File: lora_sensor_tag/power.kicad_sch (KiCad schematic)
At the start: 27 parts, among them J1 Li-ion_bat_conn, U1 MCP73871-2CAI_ML, U2 TPS63070RNMR, U3 AMS1117-3.3, U4 MAX17048G_T10

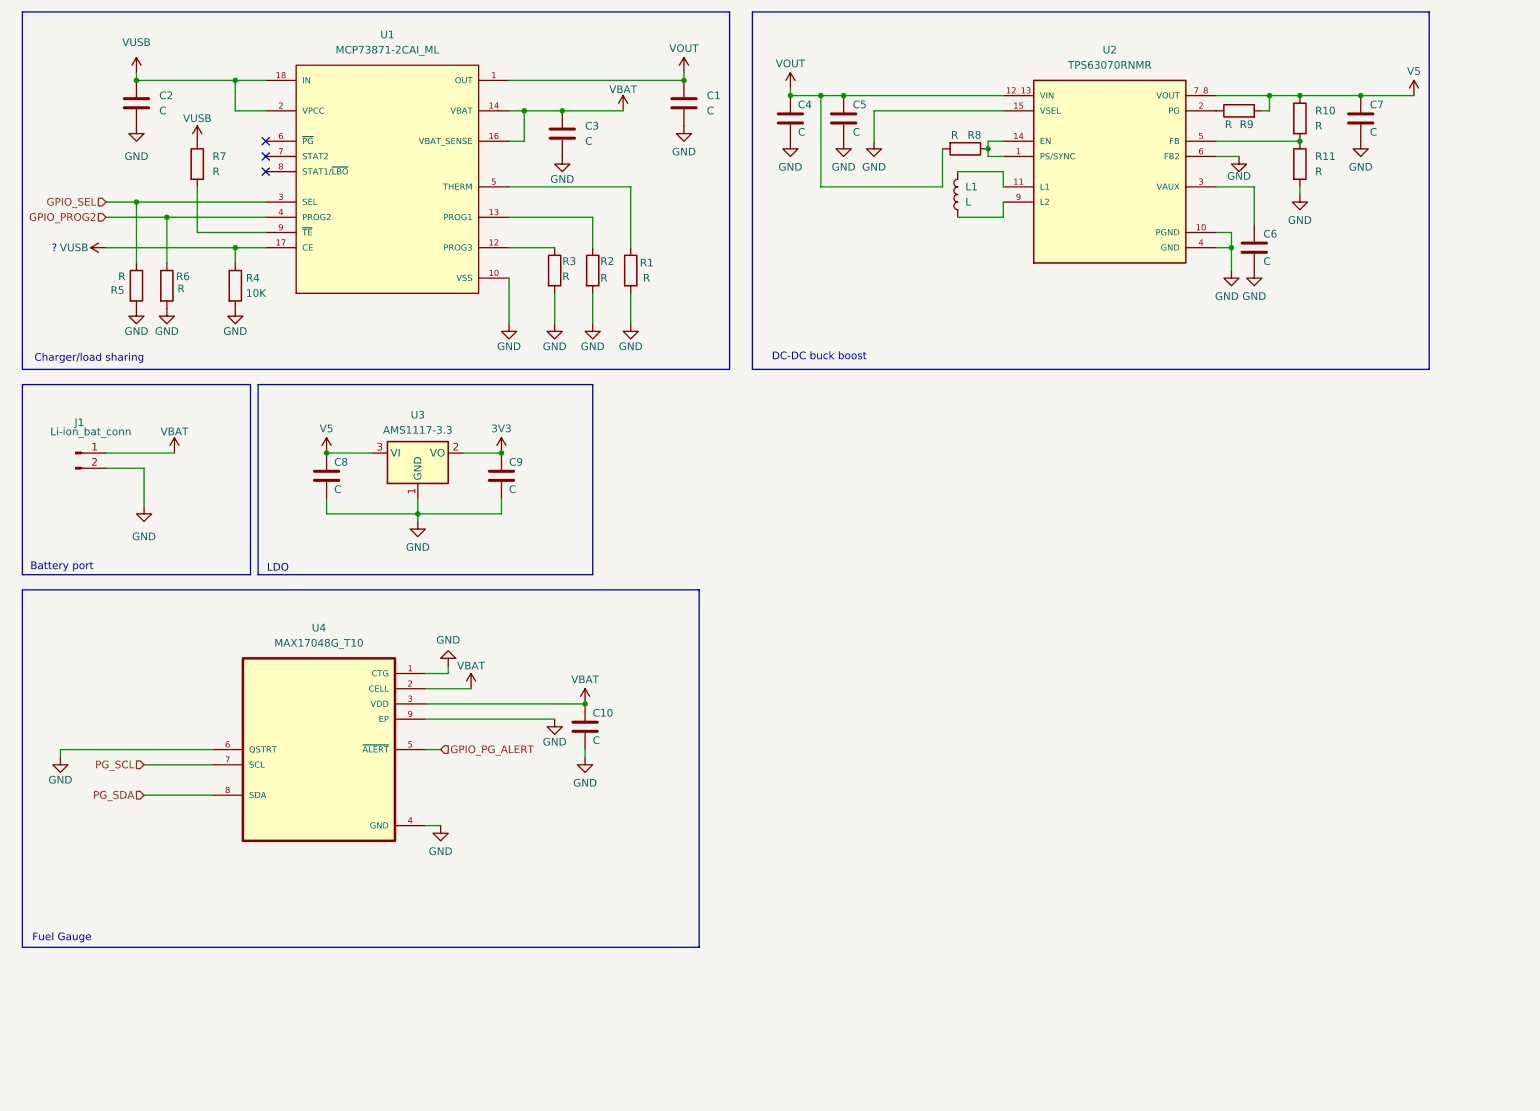
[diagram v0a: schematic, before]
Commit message: lora_sensor_tag: Update shematic
Update schematic with the following changes:
 - Add SX1276 LoRa modem schematic;
 - Add antenna matching network for SX1276 LoRa modem;
 - Add PE4259 RF switch for SX1276 LoRa modem;
 - Add USB-C connector;
 - Add CP2102 USB-to-UART bridge and programming interface;

Signed-off-by: Volodymyr <volodymyrnoha99@gmail.com>
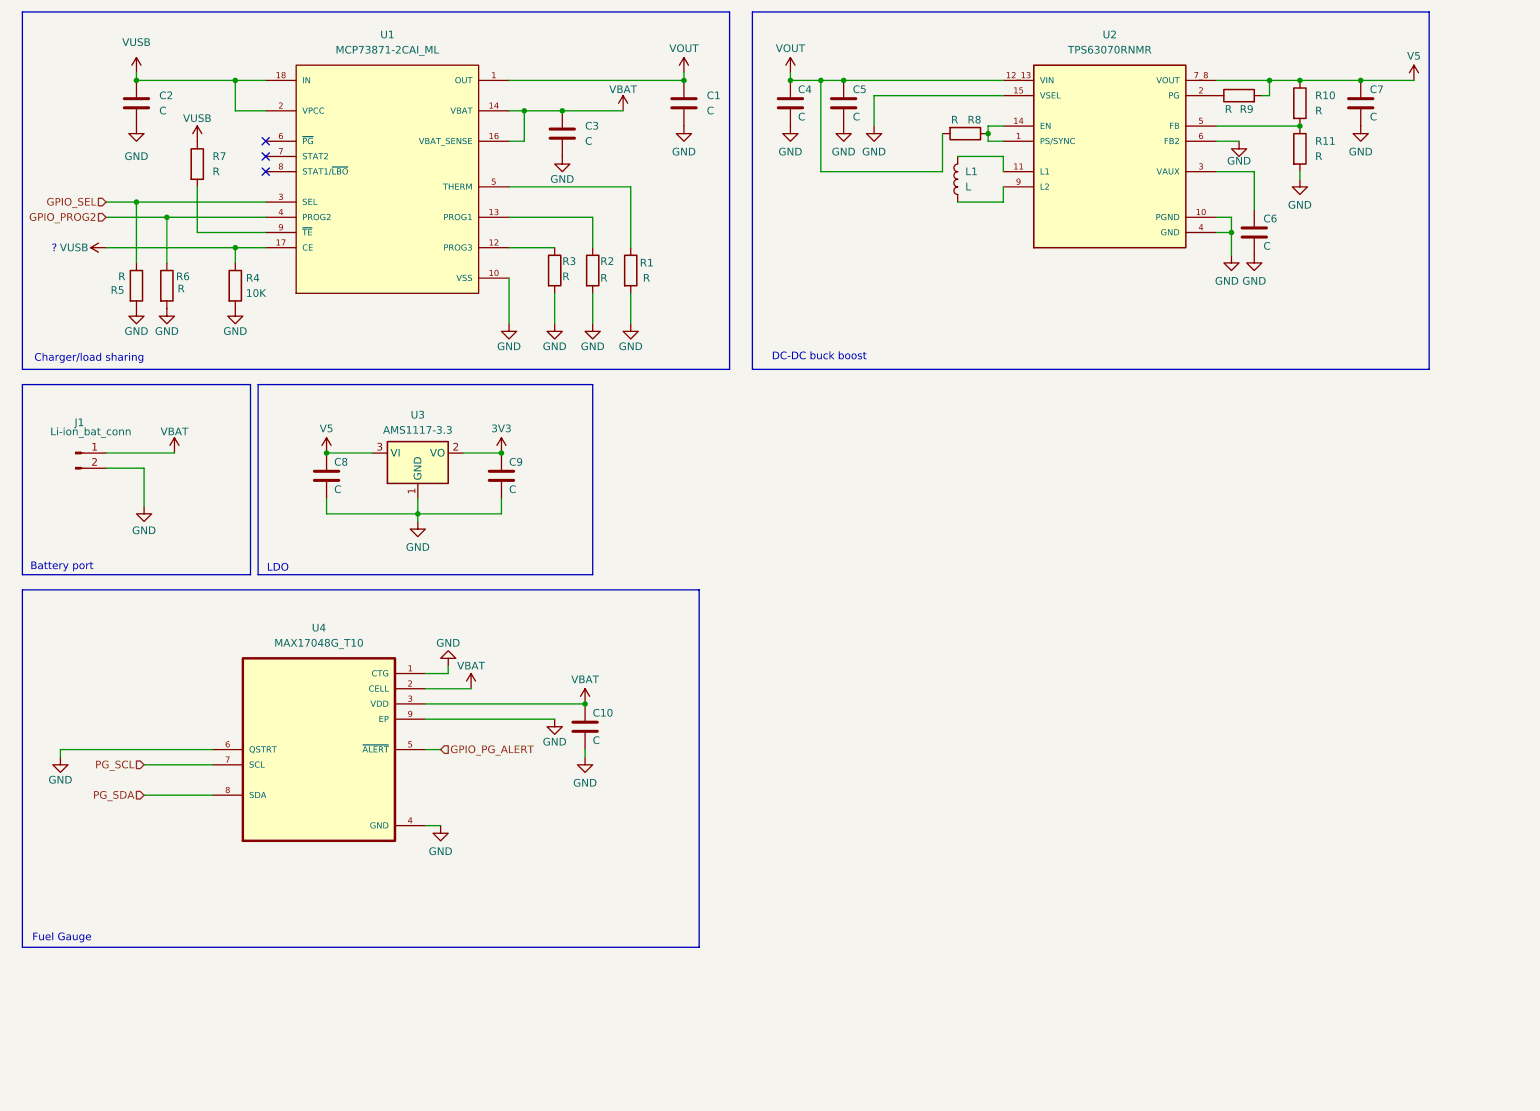
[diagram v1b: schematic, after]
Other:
- moved on the sheet: C4, C5, C6, C7, L1, R10, R11, R8, R9, U2

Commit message: Update schematic notation and fix bugs
Global labels notation updated;
Swapped line order in schematic fixed;
Added pull-up resistor to PG-ALERT pin (fuel gauge)

Signed-off-by: Volodymyr <volodymyrnoha99@gmail.com>
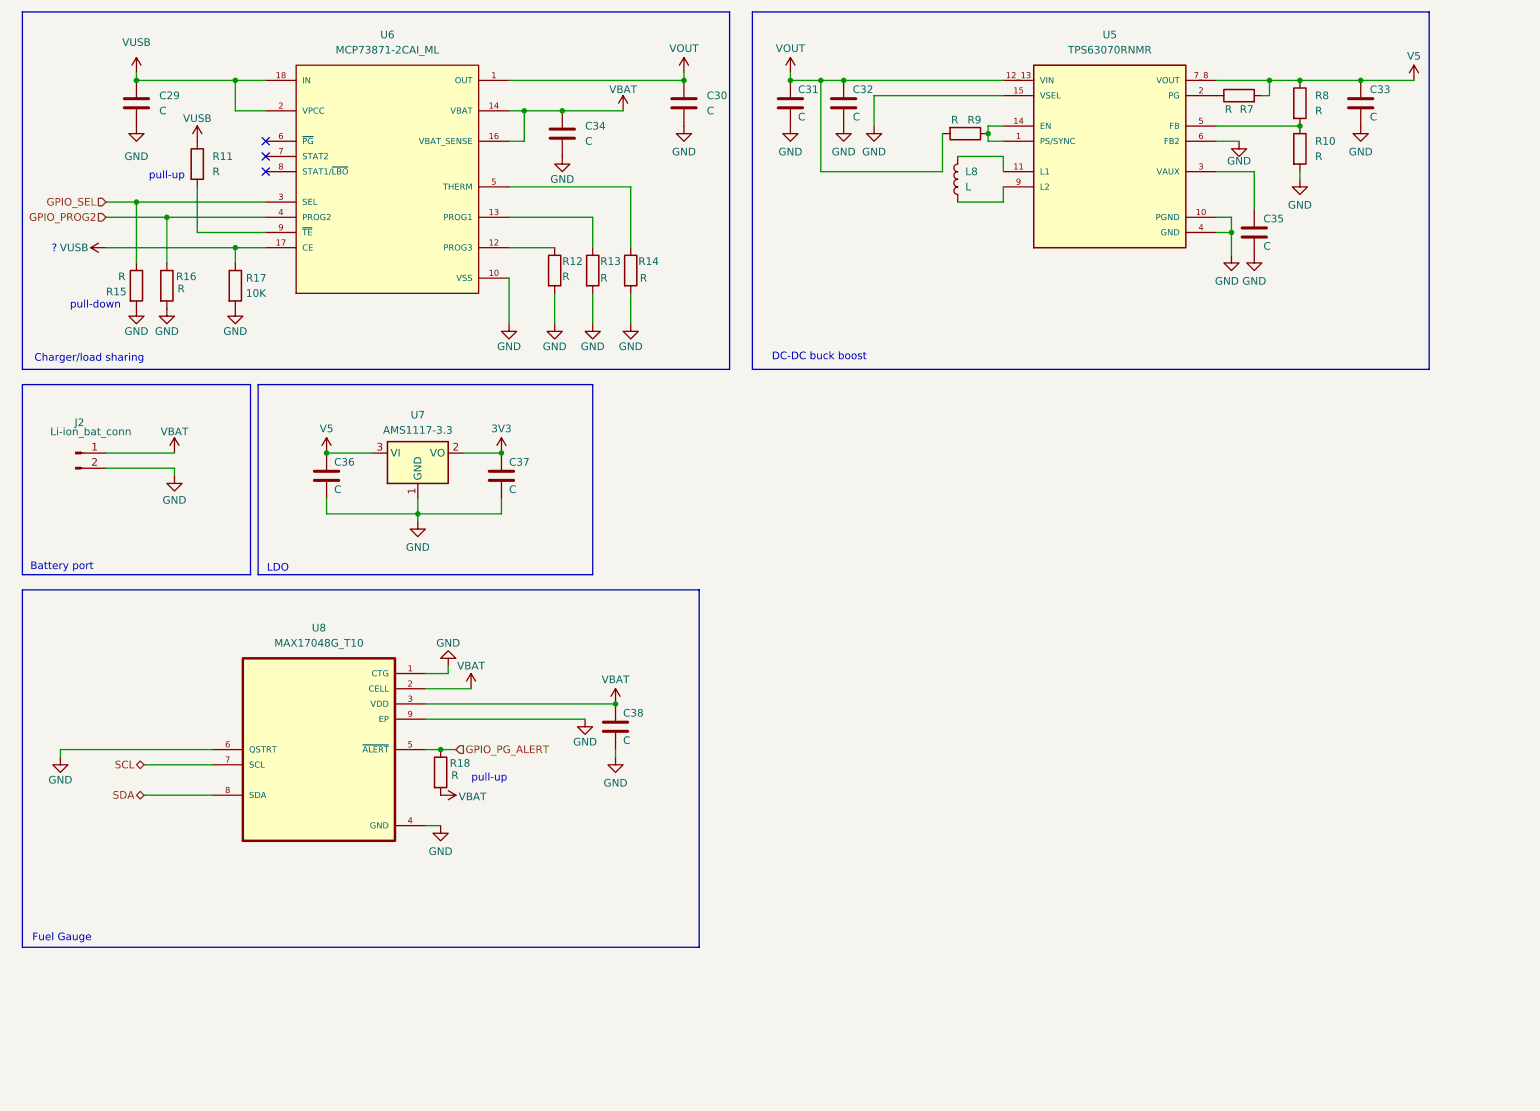
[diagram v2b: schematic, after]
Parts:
- added R18: R, TPS63070RNMR:VREG_TPS63070RNMR, symbol Device:R
- renumbered C2 to C29, C1 to C30, C4 to C31, C5 to C32, C7 to C33, C3 to C34, C6 to C35, C8 to C36, C9 to C37, C10 to C38, J1 to J2, L1 to L8, R11 to R10, R7 to R11, R3 to R12, R2 to R13, R1 to R14, R5 to R15, R6 to R16, R4 to R17, R9 to R7, R10 to R8, R8 to R9, U2 to U5, U1 to U6, U3 to U7, U4 to U8
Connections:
- net GPIO_PG_ALERT: now also R18.1
- net VBAT: now also R18.2
- net PG_SCL renamed SCL
- net PG_SDA renamed SDA
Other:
- note added: "pull-down"
- note added: "pull-up"
- title: (none) -> Power System
- moved on the sheet: C38

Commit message: Bug fixing
The following bugs and issues have been fixed:
- Fixed LoRa Rx\Tx line polarity;
- Removed unnneccessary pull-up\pull-down resistors;
- Added pull-up resistor to IO0;
- Added resistive divider for MCP7387 VPCC pin;
- GPIO_SEL moved from IO4 to IO26 (IO4 used for flash init and can cause unexpected behavior);
- CC1 and CC2 of USB-C port connected to GND via pull-down resistors;

Signed-off-by: Volodymyr <volodymyrnoha99@gmail.com>
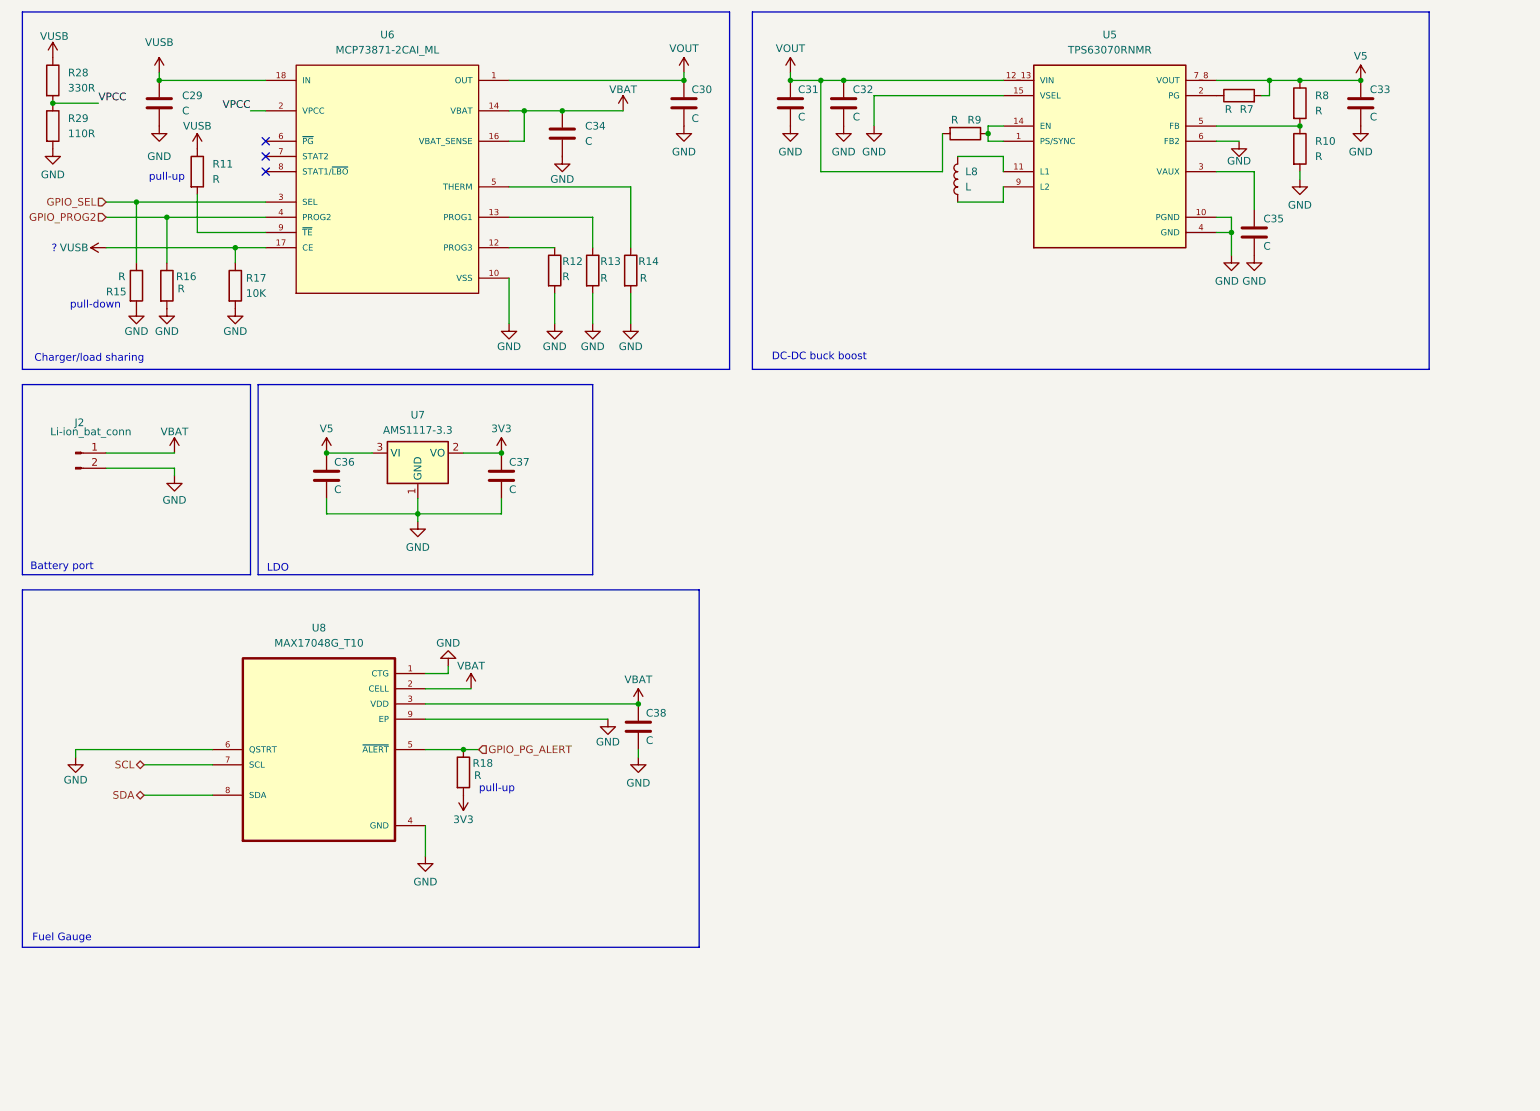
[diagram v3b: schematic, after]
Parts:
- added R28: 330R, TPS63070RNMR:VREG_TPS63070RNMR, symbol Device:R
- added R29: 110R, TPS63070RNMR:VREG_TPS63070RNMR, symbol Device:R
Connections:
- net 3V3: now also R18.2
- net GND: now also R29.2
- net VBAT: no longer R18.2
- net VUSB: now also R28.1; no longer U6.2 (VPCC)
- new net VPCC: R28.2, R29.1, U6.2 (VPCC)
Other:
- moved on the sheet: C29, C38, R11, R18

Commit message: Update Charge Enable mechanism on MCP73871
Adds the following charge enable control mechanism
on MCP73871:

VUSB ──|>|──┐
     D_CE1  │
            ├── V_CE_SRC ── R17 ──┬──── CE, U6.17
VBAT ──|>|──┘             47 кОм  │   |
     D_CE2                        C  R34
                                 │    |
GPIO26 ── R_B ──┬────────────── B Q3 GND
         47 кОм │                │
               R_BE              E   NPN
              100 кОм            │
                │               GND
               GND

This solution allows for controlled enabling of
the charge function  on the MCP73871, ensuring
that the charge enable pin is properly managed
through the diodes and transistor network.The
circuit allows control of the CE pin via the
GPIO26 pin and helps to keep CE in a proper state.

Signed-off-by: Volodymyr <volodymyrnoha99@gmail.com>
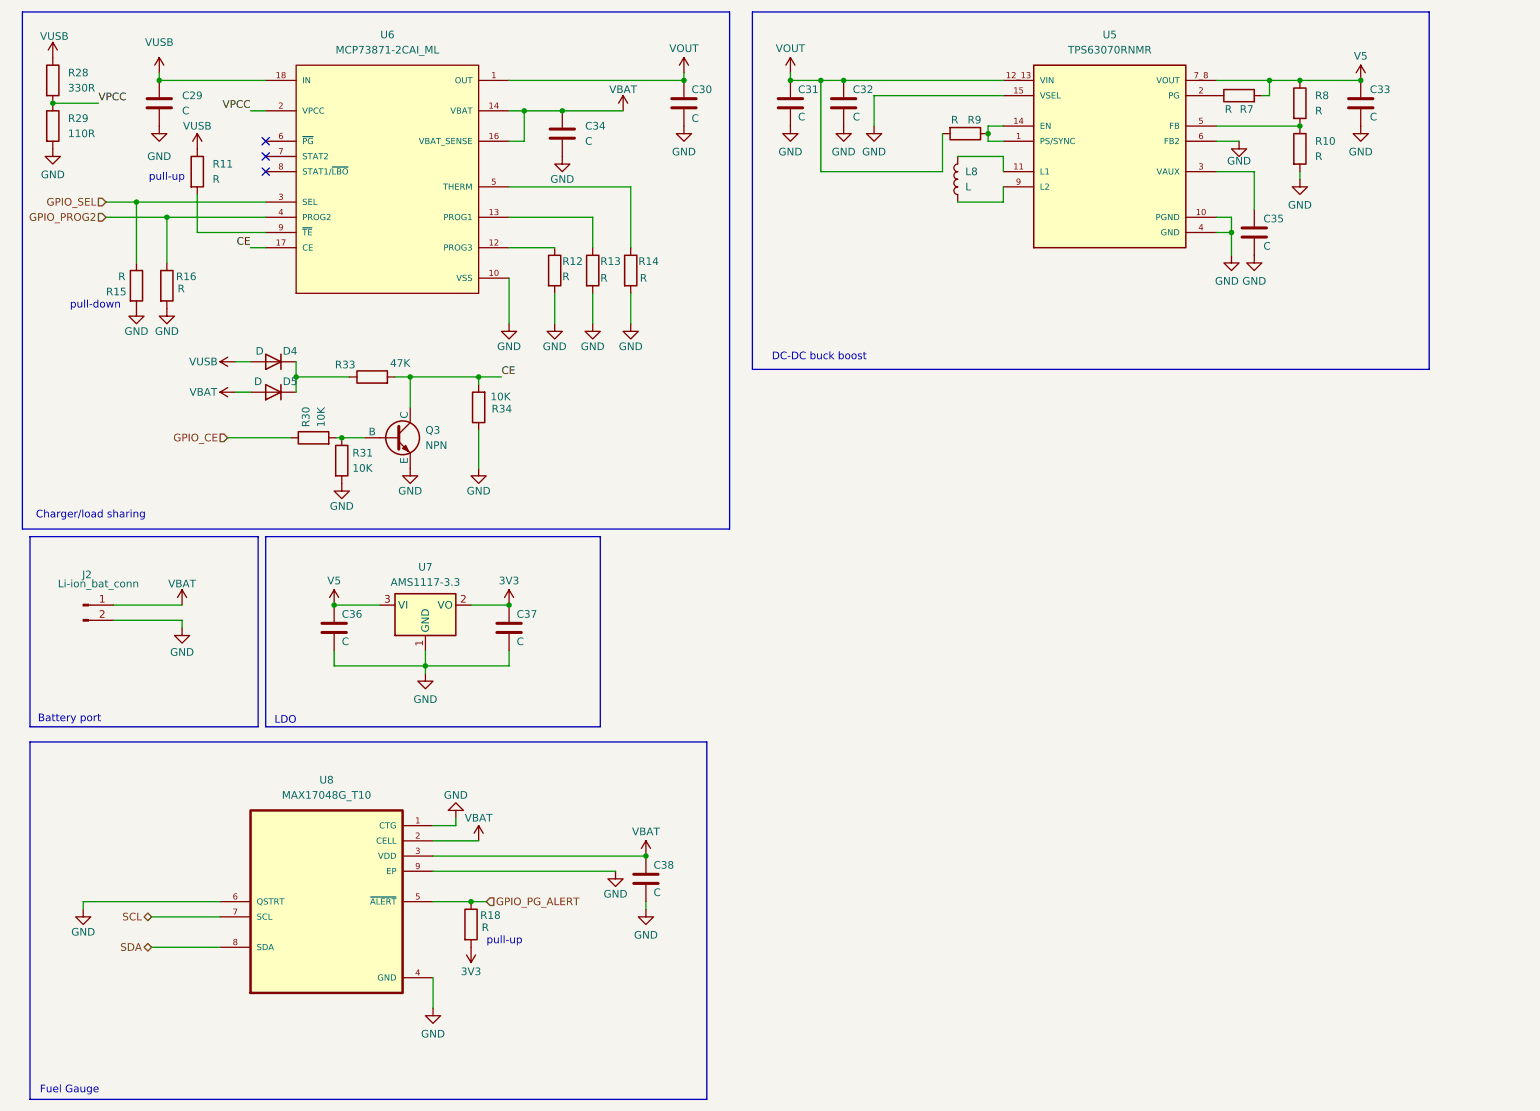
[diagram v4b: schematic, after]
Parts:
- removed R17: 10K, TPS63070RNMR:VREG_TPS63070RNMR, symbol Device:R
- added D4, D5: D, symbol Device:D
- added Q3: NPN, Package_DFN_QFN:Nordic_AQFN-94-1EP_7x7mm_P0.4mm, symbol Simulation_SPICE:NPN
- added R30, R31, R34: 10K, TPS63070RNMR:VREG_TPS63070RNMR, symbol Device:R
- added R33: 47K, TPS63070RNMR:VREG_TPS63070RNMR, symbol Device:R
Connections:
- net GND: now also Q3.3 (E), R31.2, R34.1
- net VBAT: now also D5.2 (A)
- net VUSB: now also D4.2 (A); no longer U6.17 (CE)
- new net: Q3.2 (B), R30.2, R31.1
- new net: D4.1 (K), D5.1 (K), R33.1
- new net CE: Q3.1 (C), R33.2, R34.2, U6.17 (CE)
- new net GPIO_CE: R30.1
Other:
- note removed: "?"
- moved on the sheet: C36, C37, C38, J2, R18, U7, U8
